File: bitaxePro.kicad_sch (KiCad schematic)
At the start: 90 parts, among them IC1 BM1397_mode1, J1 Conn_01x01, J2 Conn_01x01, J3 Conn_01x05, J4 Conn_01x02, J5 Conn_01x03, U1 SN74LVC1T45DRLR, U2 oscillator, U3 SN74LVC1T45DRLR, U4 SN74LVC1T45DRLR, U5 MCP1824, U6 MCP1824, U7 ESP32-C3-DEVKITC-02, U8 NCT218

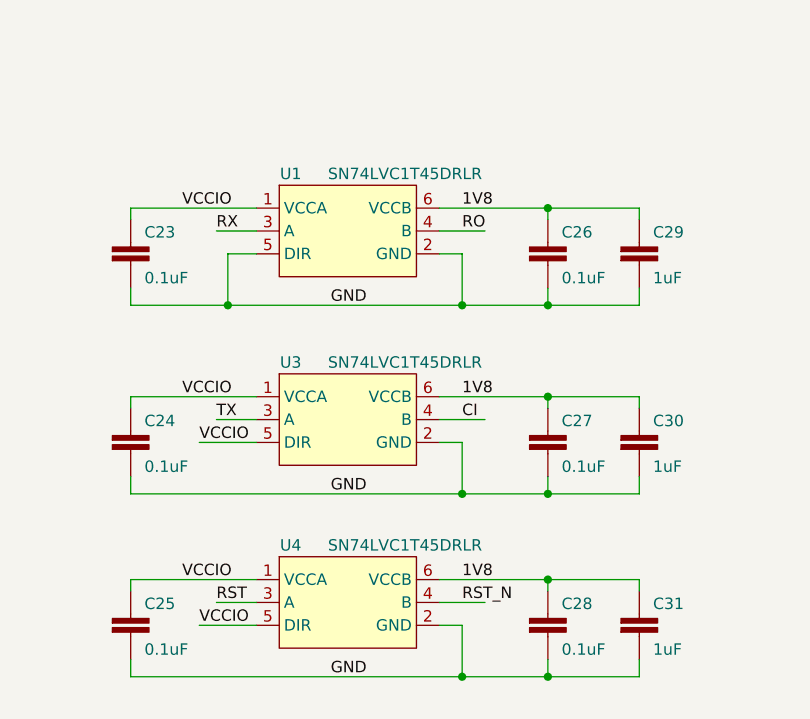
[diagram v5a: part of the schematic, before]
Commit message: switched out some OOS parts, generated BOM
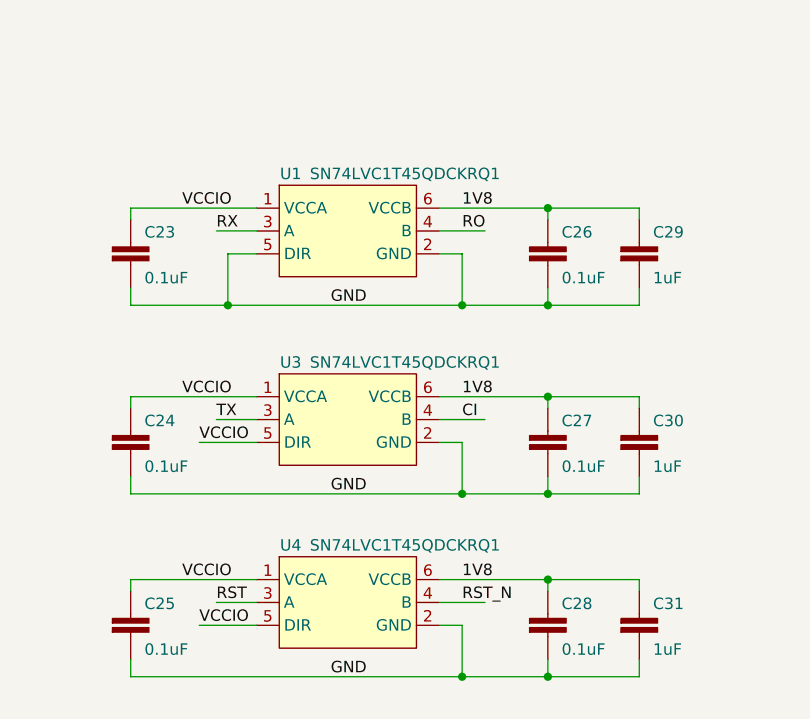
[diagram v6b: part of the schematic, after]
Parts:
- C13: DK 2388-PCT330/10DM-ND -> 718-1028-1-ND
- H1, H2, JP1, JP2: DNP (none) -> T
- H3, H4, H5, H6: footprint DayMiner:alignment_pin_1.5mm -> MountingHole:MountingHole_2.2mm_M2; DNP (none) -> T
- U1, U3, U4: value SN74LVC1T45DRLR -> SN74LVC1T45QDCKRQ1; footprint Package_TO_SOT_SMD:SOT-23-6 -> Package_TO_SOT_SMD:SOT-363_SC-70-6; DK 296-20629-1-ND -> 296-39212-1-ND; PARTNO SN74LVC1T45DRLR -> SN74LVC1T45QDCKRQ1
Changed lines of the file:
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@@
       (effects (font (size 1.27 1.27)) (justify left))
     )
-    (property "Footprint" "DayMiner:alignment_pin_1.5mm" (id 2) (at 44.45 145.415 0)
+    (property "Footprint" "MountingHole:MountingHole_2.2mm_M2" (id 2) (at 44.45 145.415 0)
       (effects (font (size 1.27 1.27)) hide)
     )
@@
     )
     (property "PARTNO" "https://www.amazon.com/dp/B07MDFS1YS" (id 4) (at 44.45 145.415 0)
+      (effects (font (size 1.27 1.27)) hide)
+    )
+    (property "DNP" "T" (id 5) (at 44.45 145.415 0)
       (effects (font (size 1.27 1.27)) hide)
     )
@@
       (effects (font (size 1.27 1.27)) hide)
     )
+    (property "DNP" "T" (id 4) (at 86.36 64.135 0)
+      (effects (font (size 1.27 1.27)) hide)
+    )
     (pin "1")
     (pin "2")
@@
     (in_bom yes) (on_board yes)
     (property "Reference" "U1" (id 0) (at 227.33 103.505 0))
-    (property "Value" "SN74LVC1T45DRLR" (id 1) (at 240.03 103.505 0))
-    (property "Footprint" "Package_TO_SOT_SMD:SOT-23-6" (id 2) (at 234.95 118.745 0)
-      (effects (font (size 1.27 1.27)) hide)
-    )
-    (property "Datasheet" "http://www.ti.com/lit/ds/symlink/sn74lvc1t45.pdf" (id 3) (at 210.82 126.365 0)
-      (effects (font (size 1.27 1.27)) hide)
-    )
-    (property "DK" "296-20629-1-ND" (id 4) (at 233.68 109.855 0)
-      (effects (font (size 1.27 1.27)) hide)
-    )
-    (property "PARTNO" "SN74LVC1T45DRLR" (id 5) (at 233.68 109.855 0)
+    (property "Value" "SN74LVC1T45QDCKRQ1" (id 1) (at 240.03 103.505 0))
+    (property "Footprint" "Package_TO_SOT_SMD:SOT-363_SC-70-6" (id 2) (at 234.95 118.745 0)
+      (effects (font (size 1.27 1.27)) hide)
+    )
+    (property "Datasheet" "https://www.ti.com/lit/ds/symlink/sn74lvc1t45-q1.pdf" (id 3) (at 210.82 126.365 0)
+      (effects (font (size 1.27 1.27)) hide)
+    )
+    (property "DK" "296-39212-1-ND" (id 4) (at 233.68 109.855 0)
+      (effects (font (size 1.27 1.27)) hide)
+    )
+    (property "PARTNO" "SN74LVC1T45QDCKRQ1" (id 5) (at 233.68 109.855 0)
       (effects (font (size 1.27 1.27)) hide)
     )
@@
     (in_bom yes) (on_board yes)
     (property "Reference" "U3" (id 0) (at 227.33 124.46 0))
-    (property "Value" "SN74LVC1T45DRLR" (id 1) (at 240.03 124.46 0))
-    (property "Footprint" "Package_TO_SOT_SMD:SOT-23-6" (id 2) (at 234.95 139.7 0)
-      (effects (font (size 1.27 1.27)) hide)
-    )
-    (property "Datasheet" "http://www.ti.com/lit/ds/symlink/sn74lvc1t45.pdf" (id 3) (at 210.82 147.32 0)
-      (effects (font (size 1.27 1.27)) hide)
-    )
-    (property "DK" "296-20629-1-ND" (id 4) (at 233.68 130.81 0)
-      (effects (font (size 1.27 1.27)) hide)
-    )
-    (property "PARTNO" "SN74LVC1T45DRLR" (id 5) (at 233.68 130.81 0)
+    (property "Value" "SN74LVC1T45QDCKRQ1" (id 1) (at 240.03 124.46 0))
+    (property "Footprint" "Package_TO_SOT_SMD:SOT-363_SC-70-6" (id 2) (at 234.95 139.7 0)
+      (effects (font (size 1.27 1.27)) hide)
+    )
+    (property "Datasheet" "https://www.ti.com/lit/ds/symlink/sn74lvc1t45-q1.pdf" (id 3) (at 210.82 147.32 0)
+      (effects (font (size 1.27 1.27)) hide)
+    )
+    (property "DK" "296-39212-1-ND" (id 4) (at 233.68 130.81 0)
+      (effects (font (size 1.27 1.27)) hide)
+    )
+    (property "PARTNO" "SN74LVC1T45QDCKRQ1" (id 5) (at 233.68 130.81 0)
       (effects (font (size 1.27 1.27)) hide)
     )
@@
       (effects (font (size 1.27 1.27)) (justify left))
     )
-    (property "Footprint" "DayMiner:alignment_pin_1.5mm" (id 2) (at 44.45 139.065 0)
+    (property "Footprint" "MountingHole:MountingHole_2.2mm_M2" (id 2) (at 44.45 139.065 0)
       (effects (font (size 1.27 1.27)) hide)
     )
@@
     )
     (property "PARTNO" "https://www.amazon.com/dp/B07MDFS1YS" (id 4) (at 44.45 139.065 0)
+      (effects (font (size 1.27 1.27)) hide)
+    )
+    (property "DNP" "T" (id 5) (at 44.45 139.065 0)
       (effects (font (size 1.27 1.27)) hide)
     )
@@
       (effects (font (size 1.27 1.27)) hide)
     )
-    (property "DK" "2388-PCT330/10DM-ND" (id 4) (at 133.35 26.67 0)
+    (property "DK" "718-1028-1-ND" (id 4) (at 133.35 26.67 0)
       (effects (font (size 1.27 1.27)) hide)
     )
@@
       (effects (font (size 1.27 1.27)) (justify left))
     )
-    (property "Footprint" "DayMiner:alignment_pin_1.5mm" (id 2) (at 44.45 132.715 0)
+    (property "Footprint" "MountingHole:MountingHole_2.2mm_M2" (id 2) (at 44.45 132.715 0)
       (effects (font (size 1.27 1.27)) hide)
     )
@@
     )
     (property "PARTNO" "https://www.amazon.com/dp/B07MDFS1YS" (id 4) (at 44.45 132.715 0)
+      (effects (font (size 1.27 1.27)) hide)
+    )
+    (property "DNP" "T" (id 5) (at 44.45 132.715 0)
       (effects (font (size 1.27 1.27)) hide)
     )
@@
       (effects (font (size 1.27 1.27)) hide)
     )
+    (property "DNP" "T" (id 4) (at 70.485 152.4 0)
+      (effects (font (size 1.27 1.27)) hide)
+    )
   )
   (symbol (lib_id "Connector:TestPoint") (at 135.89 86.995 270) (mirror x) (unit 1)
@@
     (in_bom yes) (on_board yes)
     (property "Reference" "U4" (id 0) (at 227.33 144.78 0))
-    (property "Value" "SN74LVC1T45DRLR" (id 1) (at 240.03 144.78 0))
-    (property "Footprint" "Package_TO_SOT_SMD:SOT-23-6" (id 2) (at 234.95 160.02 0)
-      (effects (font (size 1.27 1.27)) hide)
-    )
-    (property "Datasheet" "http://www.ti.com/lit/ds/symlink/sn74lvc1t45.pdf" (id 3) (at 210.82 167.64 0)
-      (effects (font (size 1.27 1.27)) hide)
-    )
-    (property "DK" "296-20629-1-ND" (id 4) (at 233.68 151.13 0)
-      (effects (font (size 1.27 1.27)) hide)
-    )
-    (property "PARTNO" "SN74LVC1T45DRLR" (id 5) (at 233.68 151.13 0)
+    (property "Value" "SN74LVC1T45QDCKRQ1" (id 1) (at 240.03 144.78 0))
+    (property "Footprint" "Package_TO_SOT_SMD:SOT-363_SC-70-6" (id 2) (at 234.95 160.02 0)
+      (effects (font (size 1.27 1.27)) hide)
+    )
+    (property "Datasheet" "https://www.ti.com/lit/ds/symlink/sn74lvc1t45-q1.pdf" (id 3) (at 210.82 167.64 0)
+      (effects (font (size 1.27 1.27)) hide)
+    )
+    (property "DK" "296-39212-1-ND" (id 4) (at 233.68 151.13 0)
+      (effects (font (size 1.27 1.27)) hide)
+    )
+    (property "PARTNO" "SN74LVC1T45QDCKRQ1" (id 5) (at 233.68 151.13 0)
       (effects (font (size 1.27 1.27)) hide)
     )
@@
     )
     (property "Datasheet" "~" (id 3) (at 70.485 144.78 0)
+      (effects (font (size 1.27 1.27)) hide)
+    )
+    (property "DNP" "T" (id 4) (at 70.485 144.78 0)
       (effects (font (size 1.27 1.27)) hide)
     )
@@
       (effects (font (size 1.27 1.27)) hide)
     )
+    (property "DNP" "T" (id 4) (at 86.36 66.675 0)
+      (effects (font (size 1.27 1.27)) hide)
+    )
     (pin "1")
     (pin "2")
@@
       (effects (font (size 1.27 1.27)) (justify left))
     )
-    (property "Footprint" "DayMiner:alignment_pin_1.5mm" (id 2) (at 44.45 152.4 0)
+    (property "Footprint" "MountingHole:MountingHole_2.2mm_M2" (id 2) (at 44.45 152.4 0)
       (effects (font (size 1.27 1.27)) hide)
     )
@@
     )
     (property "PARTNO" "https://www.amazon.com/dp/B07MDFS1YS" (id 4) (at 44.45 152.4 0)
+      (effects (font (size 1.27 1.27)) hide)
+    )
+    (property "DNP" "T" (id 5) (at 44.45 152.4 0)
       (effects (font (size 1.27 1.27)) hide)
     )
@@
     )
     (path "/a097db18-83db-4470-ba17-86144dcc33ba"
-      (reference "H3") (unit 1) (value "AlignmentHole") (footprint "DayMiner:alignment_pin_1.5mm")
+      (reference "H3") (unit 1) (value "AlignmentHole") (footprint "MountingHole:MountingHole_2.2mm_M2")
     )
     (path "/7e4cf7cf-9964-4d64-80bc-9a8d32a7cbd1"
-      (reference "H4") (unit 1) (value "AlignmentHole") (footprint "DayMiner:alignment_pin_1.5mm")
+      (reference "H4") (unit 1) (value "AlignmentHole") (footprint "MountingHole:MountingHole_2.2mm_M2")
     )
     (path "/11b3d4e8-2628-4a40-8ff8-a648827b2eb8"
-      (reference "H5") (unit 1) (value "AlignmentHole") (footprint "DayMiner:alignment_pin_1.5mm")
+      (reference "H5") (unit 1) (value "AlignmentHole") (footprint "MountingHole:MountingHole_2.2mm_M2")
     )
     (path "/f695d883-8c65-46c1-95e4-8c074a67d8cb"
-      (reference "H6") (unit 1) (value "AlignmentHole") (footprint "DayMiner:alignment_pin_1.5mm")
+      (reference "H6") (unit 1) (value "AlignmentHole") (footprint "MountingHole:MountingHole_2.2mm_M2")
     )
     (path "/c2c4c89f-d26c-46ad-8ca9-fddab83afb42"
@@
     )
     (path "/344ae6a9-1ee5-471b-96c8-2558947378a6"
-      (reference "U1") (unit 1) (value "SN74LVC1T45DRLR") (footprint "Package_TO_SOT_SMD:SOT-23-6")
+      (reference "U1") (unit 1) (value "SN74LVC1T45QDCKRQ1") (footprint "Package_TO_SOT_SMD:SOT-363_SC-70-6")
     )
     (path "/da2b1d8a-4f67-42b6-82c6-b1b3c8edd2d0"
@@
     )
     (path "/54cdb1b8-72d1-42bd-adec-3a319c5dcfa8"
-      (reference "U3") (unit 1) (value "SN74LVC1T45DRLR") (footprint "Package_TO_SOT_SMD:SOT-23-6")
+      (reference "U3") (unit 1) (value "SN74LVC1T45QDCKRQ1") (footprint "Package_TO_SOT_SMD:SOT-363_SC-70-6")
     )
     (path "/b1235c33-780e-4d93-b27e-d7c8f108135e"
-      (reference "U4") (unit 1) (value "SN74LVC1T45DRLR") (footprint "Package_TO_SOT_SMD:SOT-23-6")
+      (reference "U4") (unit 1) (value "SN74LVC1T45QDCKRQ1") (footprint "Package_TO_SOT_SMD:SOT-363_SC-70-6")
     )
     (path "/95aa231c-7867-4f1e-9a7d-7397c0c40616"
